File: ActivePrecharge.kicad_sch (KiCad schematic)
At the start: 44 parts, among them IC1 1769205241, J1 Conn_01x03, J2 Conn_01x03, J3 Conn_01x02, Q1 Q_PMOS_GDS, Q2 IRLML0030, Q3 IRLML0030, U1 Nucleo_L432KC

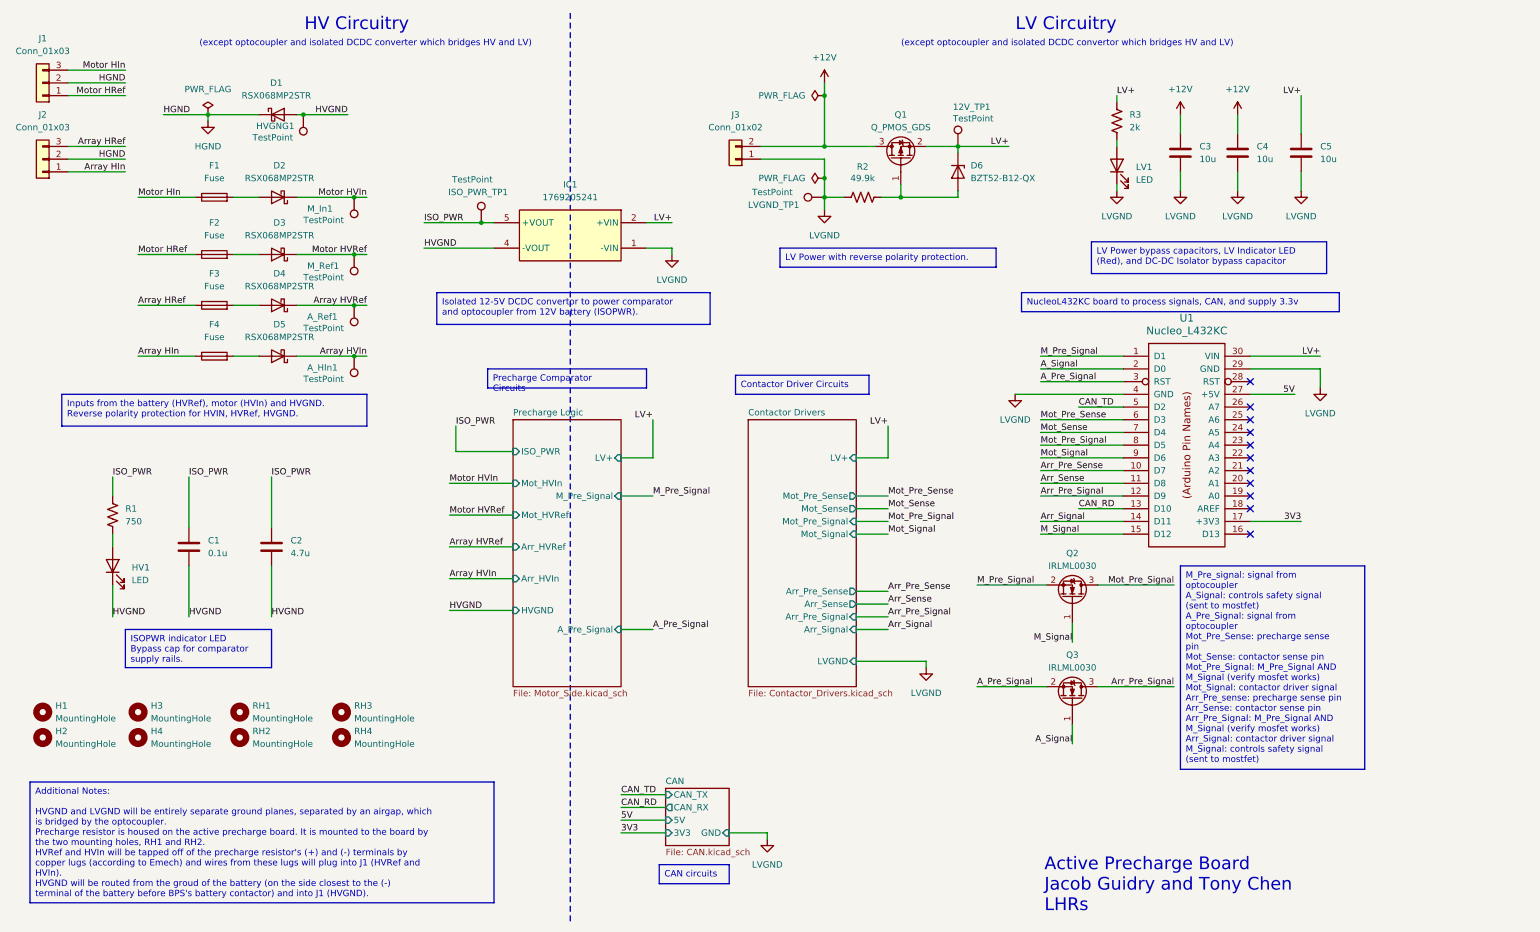
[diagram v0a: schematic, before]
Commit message: started on HV layout
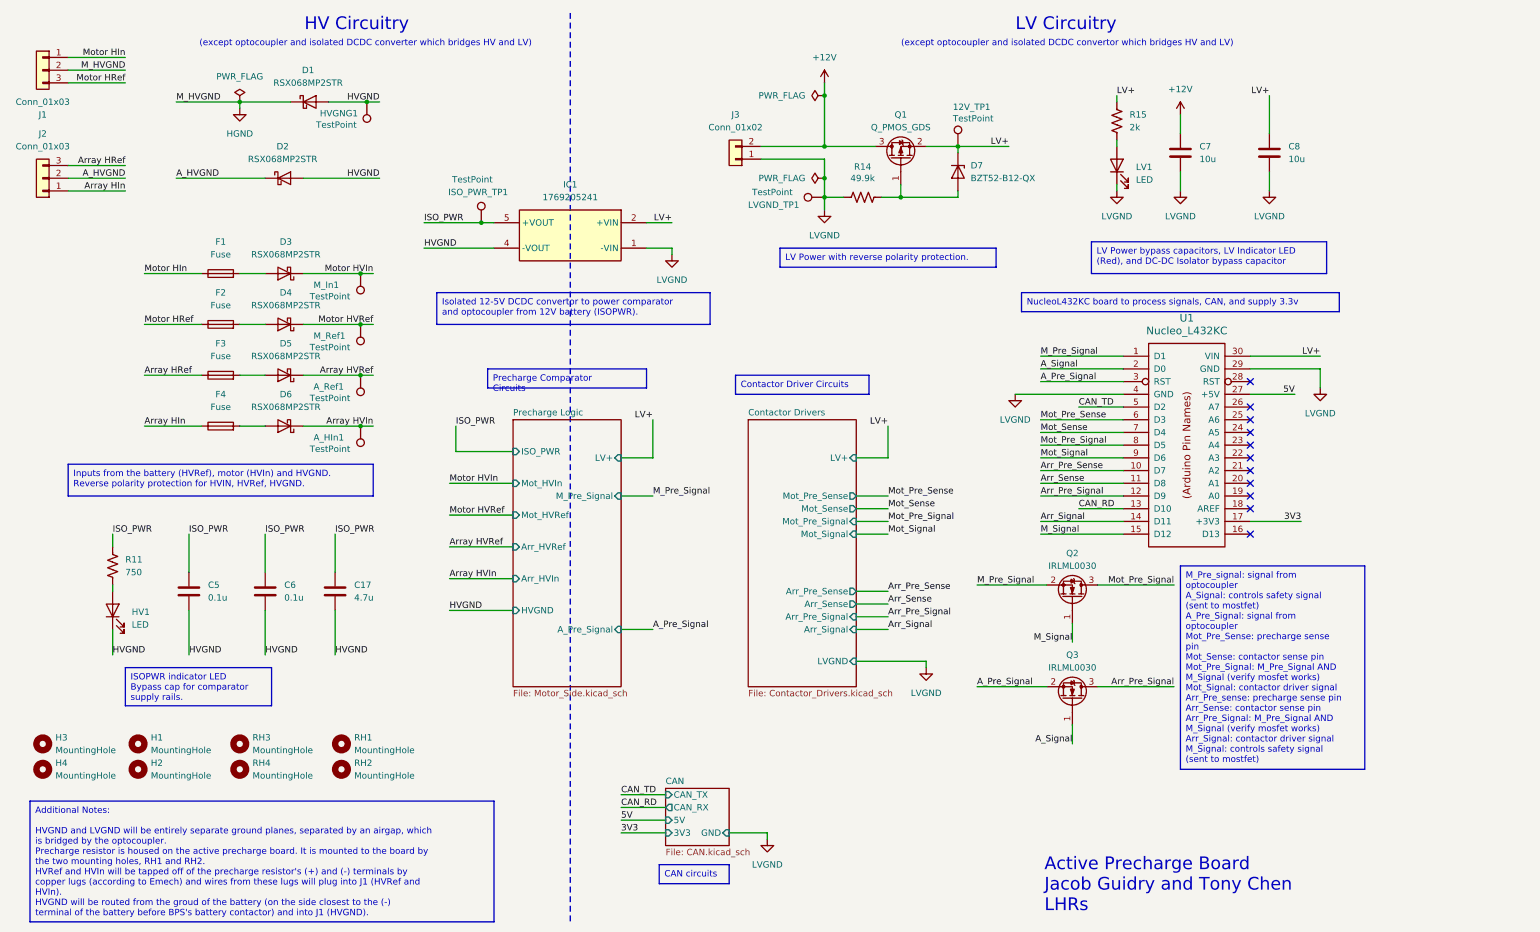
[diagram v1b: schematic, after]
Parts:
- removed C4: 10u, Capacitor_SMD:C_0805_2012Metric, symbol Device:C
- added C6: 0.1u, Capacitor_SMD:C_0805_2012Metric, symbol Device:C
- added D2: RSX068MP2STR, Diode_SMD:D_SOD-123F, symbol Device:D_Schottky
- J3: footprint (none) -> utsvt-conn:Molex_MicroFit3.0_1x2xP3.00mm_PolarizingPeg_Vertical
- renumbered C2 to C17, C1 to C5, C3 to C7, C5 to C8, D2 to D3, D3 to D4, D4 to D5, D5 to D6, D6 to D7, H3 to H1, H4 to H2, H1 to H3, H2 to H4, R1 to R11, R2 to R14, R3 to R15, RH3 to RH1, RH4 to RH2, RH1 to RH3, RH2 to RH4
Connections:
- net HGND: no longer J2.2 (Pin_2)
- net HVGND: now also C6.2, D2.2 (A)
- net ISO_PWR: now also C6.1
- net Motor HIn: now also J1.1 (Pin_1); no longer J1.3 (Pin_3)
- net Motor HRef: now also J1.3 (Pin_3); no longer J1.1 (Pin_1)
- new net A_HVGND: D2.1 (K), J2.2 (Pin_2)
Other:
- moved on the sheet: A_HIn1, A_Ref1, C17, C5, C8, D1, D3, D4, D5, D6, F1, F2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

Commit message: changed labels
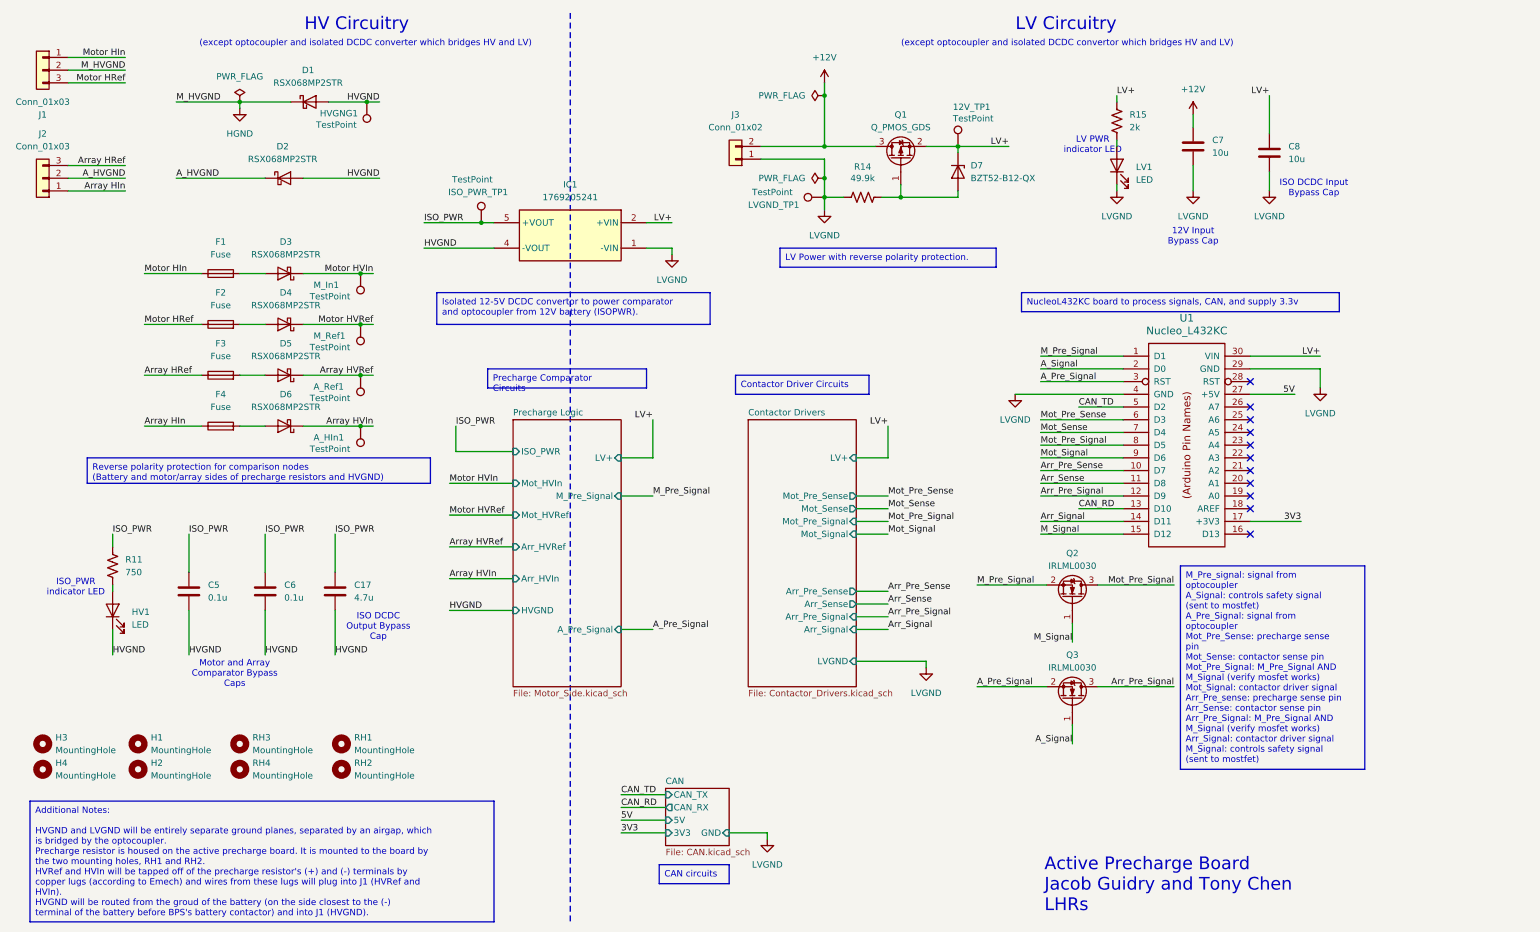
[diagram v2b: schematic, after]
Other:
- note added: "12V Input Bypass Cap"
- note added: "ISO DCDC Input Bypass Cap"
- note added: "ISO DCDC Output Bypass Cap"
- note added: "ISO_PWR indicator LED"
- note added: "LV PWR indicator LED"
- note added: "Motor and Array Comparator Bypass Caps"
- moved on the sheet: C7
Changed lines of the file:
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@@
 	(wire
 		(pts
-			(xy 247.65 34.29) (xy 247.65 38.1)
+			(xy 250.19 34.29) (xy 250.19 36.83)
 		)
 		(stroke
@@
 	(wire
 		(pts
-			(xy 247.65 45.72) (xy 247.65 49.53)
+			(xy 250.19 44.45) (xy 250.19 49.53)
 		)
 		(stroke
@@
 		)
 	)
-	(text_box "LV Power bypass capacitors, LV Indicator LED (Red), and DC-DC Isolator bypass capacitor"
-		(exclude_from_sim no)
-		(at 229.87 59.69 0)
-		(size 46.99 6.35)
-		(stroke
-			(width 0)
-			(type default)
-		)
-		(fill
-			(type none)
-		)
-		(effects
-			(font
-				(size 1.27 1.27)
-			)
-			(justify left top)
-		)
-	)
 	(text_box "Additional Notes:\n\nHVGND and LVGND will be entirely separate ground planes, separated by an airgap, which is bridged by the optocoupler.\nPrecharge resistor is housed on the active precharge board. It is mounted to the board by the two mounting holes, RH1 and RH2.\nHVRef and HVIn will be tapped off of the precharge resistor's (+) and (-) terminals by copper lugs (according to Emech) and wires from these lugs will plug into J1 (HVRef and HVIn).\nHVGND will be routed from the groud of the battery (on the side closest to the (-) terminal of the battery before BPS's battery contactor) and into J1 (HVGND)."
 		(exclude_from_sim no)
@@
 		)
 	)
-	(text_box "ISOPWR indicator LED\nBypass cap for comparator supply rails."
-		(exclude_from_sim no)
-		(at 36.83 144.78 0)
-		(size 29.21 7.62)
-		(stroke
-			(width 0)
-			(type default)
-		)
-		(fill
-			(type none)
-		)
-		(effects
-			(font
-				(size 1.27 1.27)
-			)
-			(justify left top)
-		)
-	)
 	(text_box "CAN circuits"
 		(exclude_from_sim no)
@@
 		)
 	)
-	(text_box "Inputs from the battery (HVRef), motor (HVIn) and HVGND.\nReverse polarity protection for HVIN, HVRef, HVGND."
+	(text_box "Reverse polarity protection for comparison nodes \n(Battery and motor/array sides of precharge resistors and HVGND)"
 		(exclude_from_sim no)
-		(at 25.4 104.14 0)
-		(size 60.96 6.35)
+		(at 29.21 102.87 0)
+		(size 68.58 5.08)
 		(stroke
 			(width 0)
@@
 		)
 	)
+	(text "ISO DCDC Input \nBypass Cap"
+		(exclude_from_sim no)
+		(at 274.32 49.022 0)
+		(effects
+			(font
+				(size 1.27 1.27)
+			)
+		)
+	)
+	(text "ISO DCDC \nOutput Bypass\nCap"
+		(exclude_from_sim no)
+		(at 87.376 136.652 0)
+		(effects
+			(font
+				(size 1.27 1.27)
+			)
+		)
+	)
 	(text "HV Circuitry"
 		(exclude_from_sim no)
@@
 		)
 	)
+	(text "LV PWR \nindicator LED"
+		(exclude_from_sim no)
+		(at 230.124 40.386 0)
+		(effects
+			(font
+				(size 1.27 1.27)
+			)
+		)
+	)
+	(text "Motor and Array\nComparator Bypass\nCaps"
+		(exclude_from_sim no)
+		(at 58.674 146.05 0)
+		(effects
+			(font
+				(size 1.27 1.27)
+			)
+		)
+	)
 	(text "(except optocoupler and isolated DCDC convertor which bridges HV and LV)"
 		(exclude_from_sim no)
@@
 		)
 	)
+	(text "12V Input\nBypass Cap"
+		(exclude_from_sim no)
+		(at 250.19 58.674 0)
+		(effects
+			(font
+				(size 1.27 1.27)
+			)
+		)
+	)
+	(text "ISO_PWR \nindicator LED"
+		(exclude_from_sim no)
+		(at 26.924 128.778 0)
+		(effects
+			(font
+				(size 1.27 1.27)
+			)
+		)
+	)
 	(text "Active Precharge Board\nJacob Guidry and Tony Chen\nLHRs\n"
 		(exclude_from_sim no)
@@
 	(symbol
 		(lib_id "power:+12V")
-		(at 247.65 34.29 0)
+		(at 250.19 34.29 0)
 		(unit 1)
 		(exclude_from_sim no)
@@
 		(fields_autoplaced yes)
 		(property "Reference" "#PWR08"
-			(at 247.65 38.1 0)
+			(at 250.19 38.1 0)
 			(effects
 				(font
@@
 		)
 		(property "Value" "+12V"
-			(at 247.65 29.21 0)
+			(at 250.19 29.21 0)
 			(effects
 				(font
@@
 		)
 		(property "Footprint" ""
-			(at 247.65 34.29 0)
+			(at 250.19 34.29 0)
 			(effects
 				(font
@@
 		)
 		(property "Datasheet" ""
-			(at 247.65 34.29 0)
+			(at 250.19 34.29 0)
 			(effects
 				(font
@@
 		)
 		(property "Description" "Power symbol creates a global label with name \"+12V\""
-			(at 247.65 34.29 0)
+			(at 250.19 34.29 0)
 			(effects
 				(font
@@
 	(symbol
 		(lib_id "Device:C")
-		(at 247.65 41.91 0)
+		(at 250.19 40.64 0)
 		(unit 1)
 		(exclude_from_sim no)
@@
 		(fields_autoplaced yes)
 		(property "Reference" "C7"
-			(at 251.46 40.6399 0)
+			(at 254 39.3699 0)
 			(effects
 				(font
@@
 		)
 		(property "Value" "10u"
-			(at 251.46 43.1799 0)
+			(at 254 41.9099 0)
 			(effects
 				(font
@@
 		)
 		(property "Footprint" "Capacitor_SMD:C_0805_2012Metric"
-			(at 248.6152 45.72 0)
+			(at 251.1552 44.45 0)
 			(effects
 				(font
@@
 		)
 		(property "Datasheet" "~"
-			(at 247.65 41.91 0)
+			(at 250.19 40.64 0)
 			(effects
 				(font
@@
 		)
 		(property "Description" "Unpolarized capacitor"
-			(at 247.65 41.91 0)
+			(at 250.19 40.64 0)
 			(effects
 				(font
@@
 	(symbol
 		(lib_id "power:GND")
-		(at 247.65 49.53 0)
+		(at 250.19 49.53 0)
 		(unit 1)
 		(exclude_from_sim no)
@@
 		(fields_autoplaced yes)
 		(property "Reference" "#PWR09"
-			(at 247.65 55.88 0)
+			(at 250.19 55.88 0)
 			(effects
 				(font
@@
 		)
 		(property "Value" "LVGND"
-			(at 247.65 54.61 0)
+			(at 250.19 54.61 0)
 			(effects
 				(font
@@
 		)
 		(property "Footprint" ""
-			(at 247.65 49.53 0)
+			(at 250.19 49.53 0)
 			(effects
 				(font
@@
 		)
 		(property "Datasheet" ""
-			(at 247.65 49.53 0)
+			(at 250.19 49.53 0)
 			(effects
 				(font
@@
 		)
 		(property "Description" "Power symbol creates a global label with name \"GND\" , ground"
-			(at 247.65 49.53 0)
+			(at 250.19 49.53 0)
 			(effects
 				(font

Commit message: fixed lakshay and ravi comments, renamed signals to be more readable, further worked on HV side layout
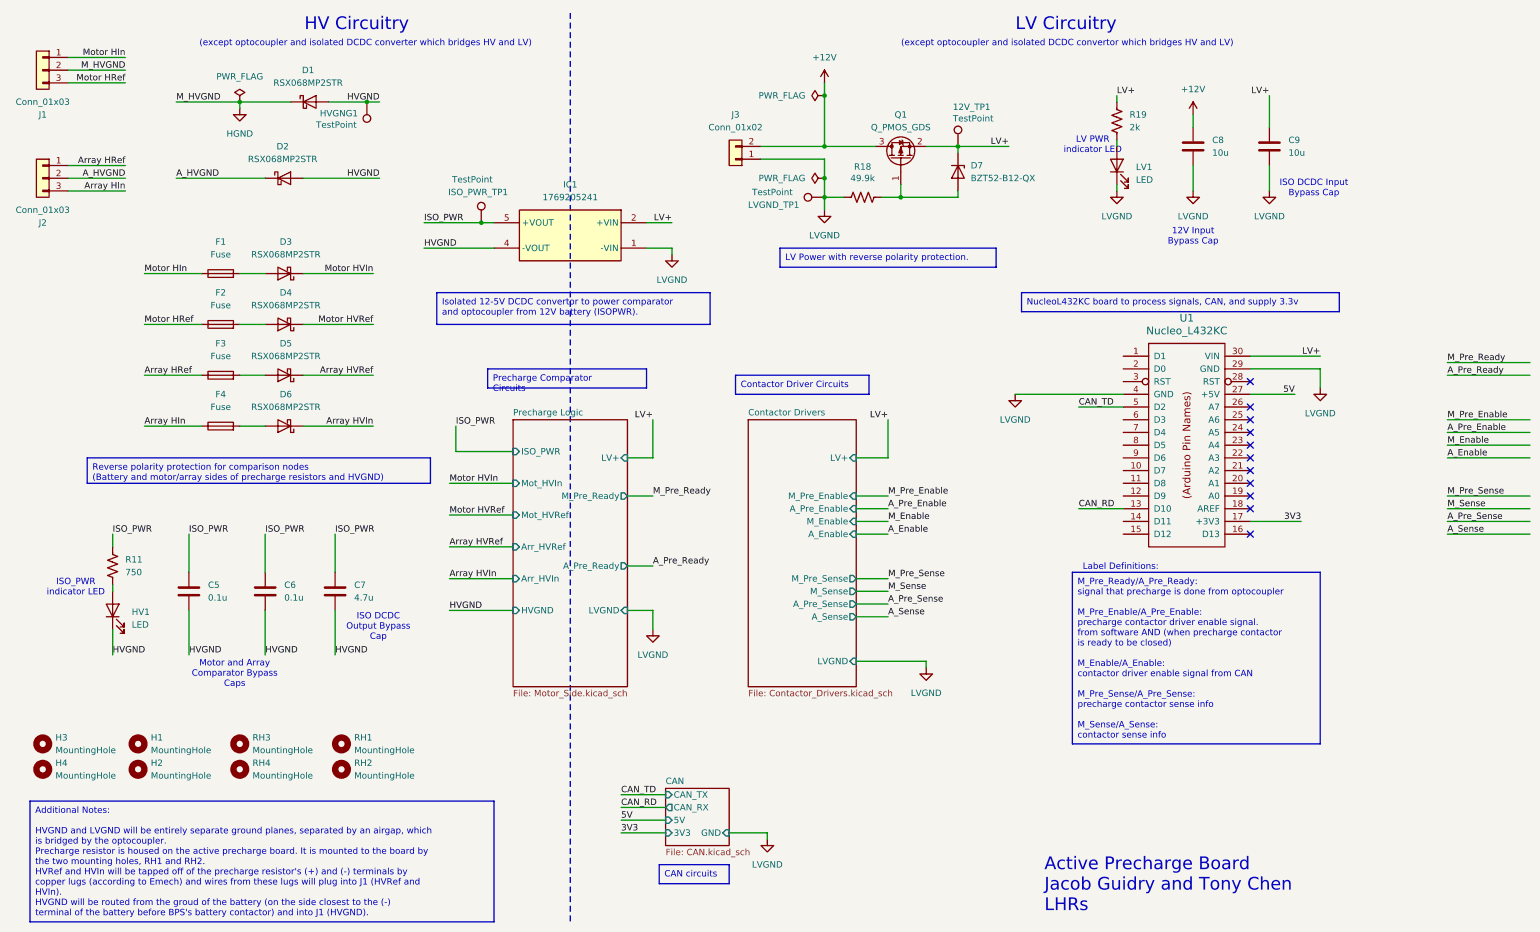
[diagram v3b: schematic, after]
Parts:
- removed A_HIn1, A_Ref1, M_In1, M_Ref1: TestPoint, utsvt-special:TestPoint_HEX_3mmID, symbol Connector:TestPoint
- removed Q2, Q3: IRLML0030, Package_TO_SOT_SMD:SOT-23, symbol Transistor_FET:IRLML0030
- renumbered C17 to C7, C7 to C8, C8 to C9, R14 to R18, R15 to R19
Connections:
- net Array HIn: now also J2.3 (Pin_3); no longer J2.1 (Pin_1)
- net Array HRef: now also J2.1 (Pin_1); no longer J2.3 (Pin_3)
- net A_Pre_Signal: no longer names the net of U1.3 (RST)
- net A_Signal: no longer names the net of U1.2 (D0)
- net Arr_Pre_Sense: no longer names the net of U1.10 (D7)
- net Arr_Pre_Signal: no longer names the net of U1.12 (D9)
- net Arr_Sense: no longer names the net of U1.11 (D8)
- net Arr_Signal: no longer names the net of U1.14 (D11)
- net M_Pre_Signal: no longer names the net of U1.1 (D1)
- net M_Signal: no longer names the net of U1.15 (D12)
- net Mot_Pre_Sense: no longer names the net of U1.6 (D3)
- net Mot_Pre_Signal: no longer names the net of U1.8 (D5)
- net Mot_Sense: no longer names the net of U1.7 (D4)
- net Mot_Signal: no longer names the net of U1.9 (D6)
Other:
- sheet Contactor Drivers ports: added A_Enable, A_Pre_Enable, A_Pre_Sense, A_Sense, M_Enable, M_Pre_Enable, M_Pre_Sense, M_Sense; removed Arr_Pre_Sense, Arr_Pre_Signal, Arr_Sense, Arr_Signal, Mot_Pre_Sense, Mot_Pre_Signal, Mot_Sense, Mot_Signal
- sheet Precharge Logic ports: added A_Pre_Ready, LVGND, M_Pre_Ready; removed A_Pre_Signal, M_Pre_Signal
- note added: "Label Definitions:"
- moved on the sheet: C9, J2

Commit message: end of workday, will work on more tonight
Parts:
- removed H3, H4: MountingHole, MountingHole:MountingHole_3mm, symbol Mechanical:MountingHole
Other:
- moved on the sheet: C5, C6, C7, D3, D4, D5, D6, F1, F2, F3, F4, HV1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
